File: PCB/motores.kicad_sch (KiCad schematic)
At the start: 30 parts, among them IC2 IR2175STRPBF, J10 Conn_01x03, J11 Conn_01x03, J12 motor_dc, J9 motor_lineal, K1 G6E, K2 G6E, K3 G6E, K4 G6E, Q1 AO3401A, Q2 AO3401A, Q3 AO3401A, Q4 AO3401A

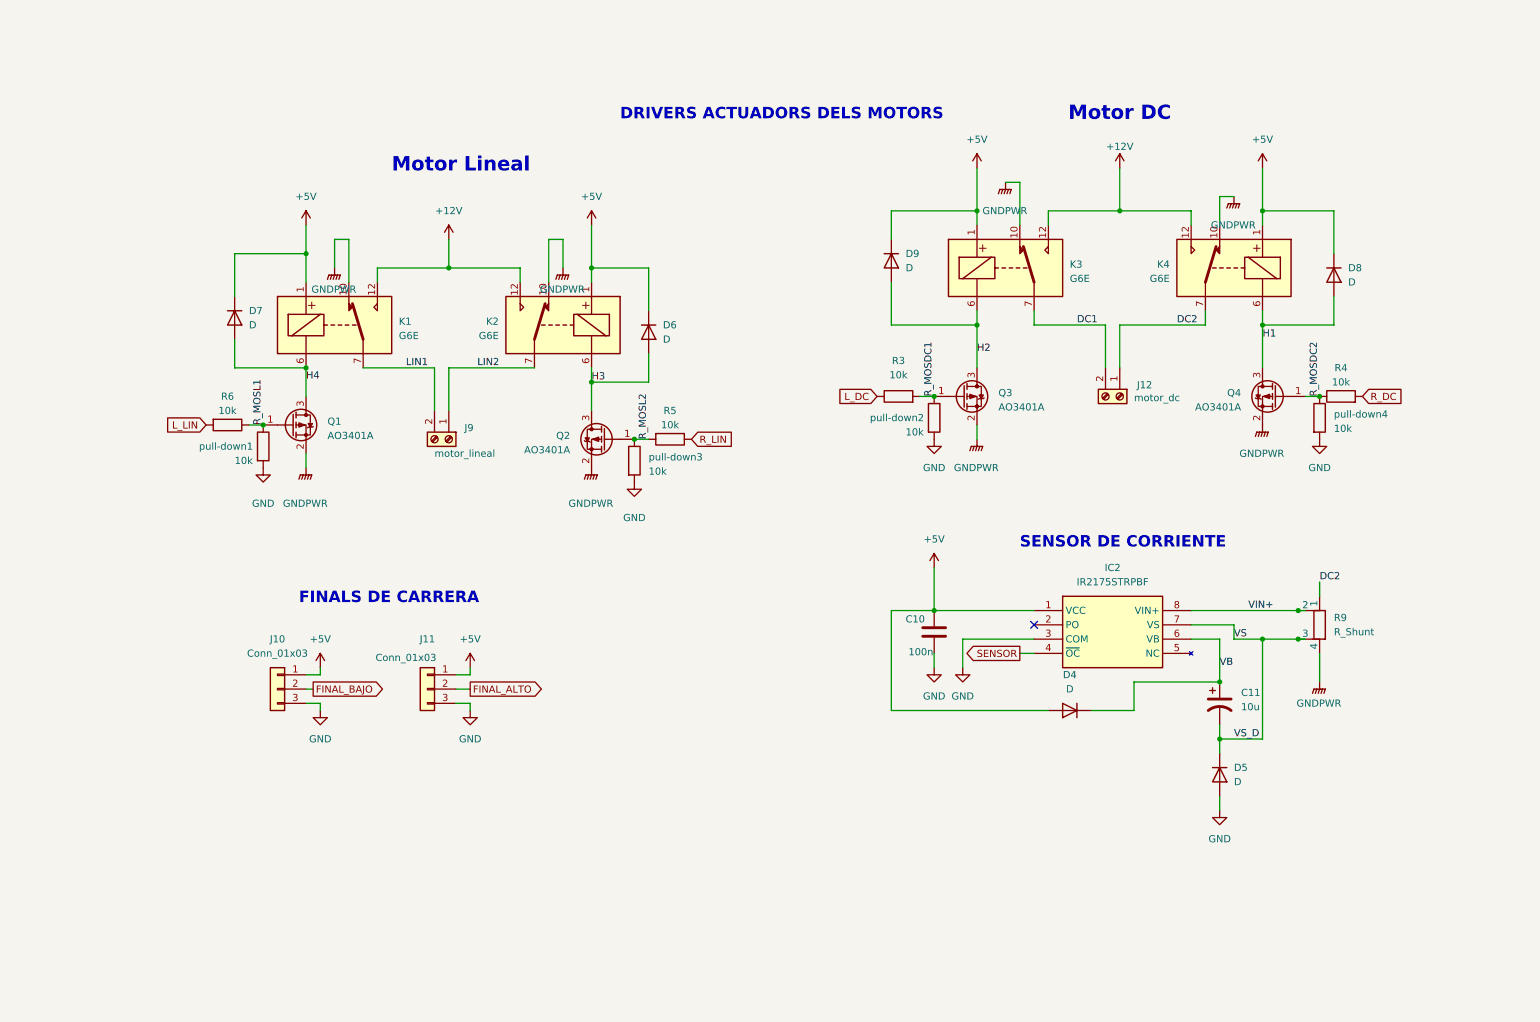
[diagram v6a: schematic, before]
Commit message: Fixed motors
mosfet shcematic fix
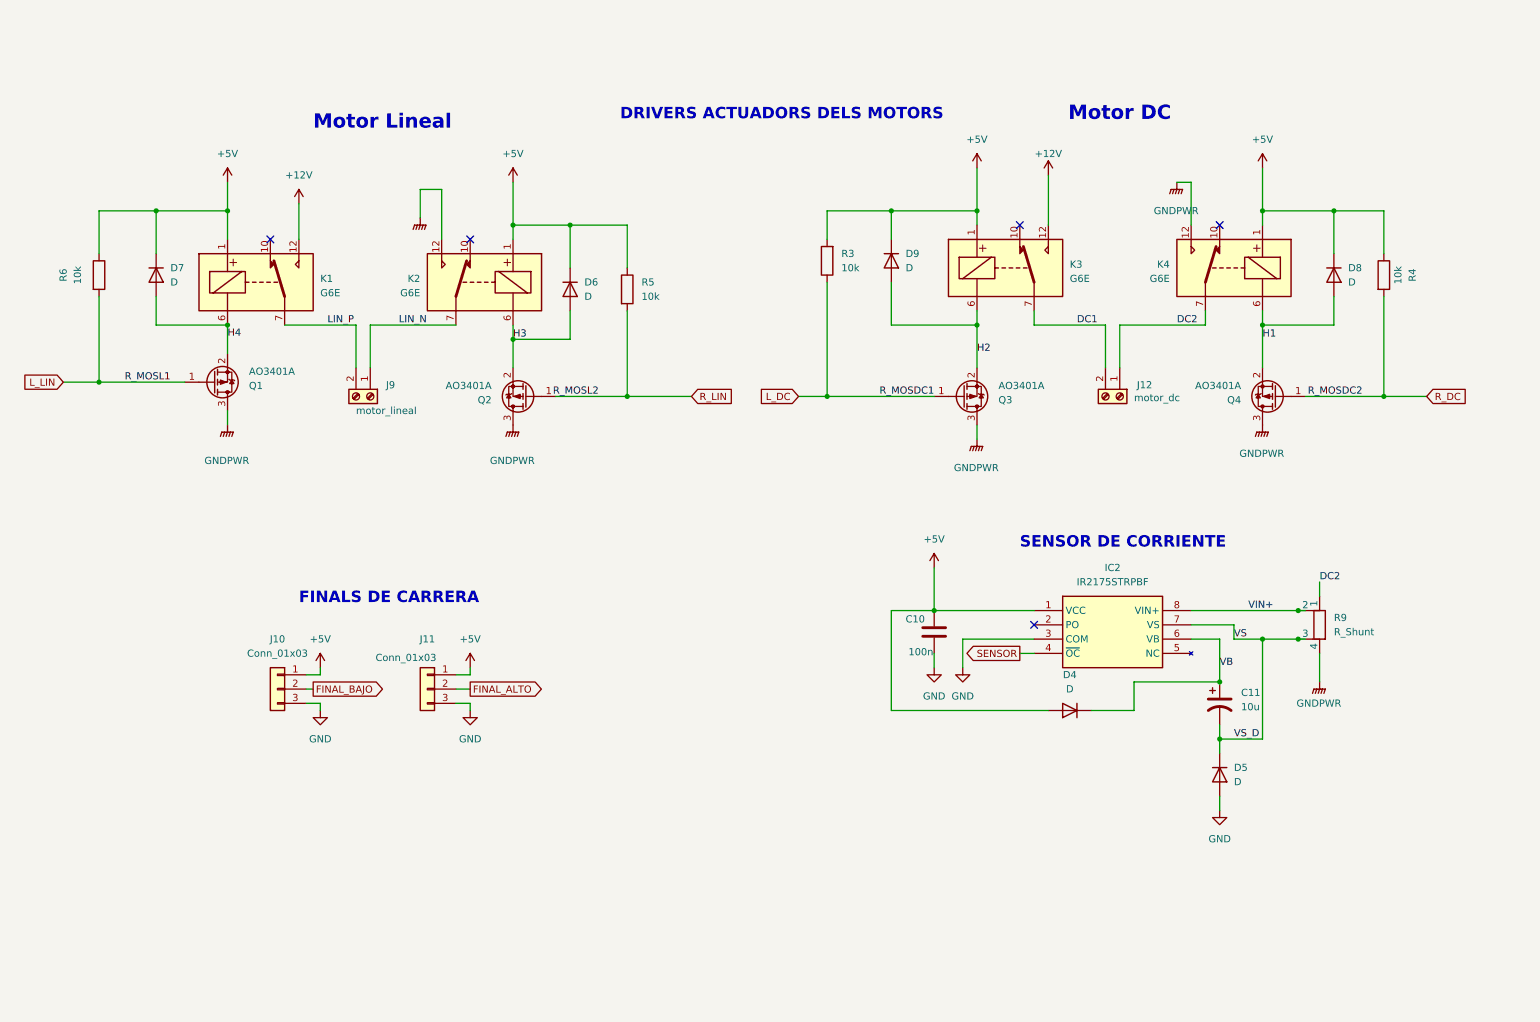
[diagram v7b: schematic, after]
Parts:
- removed pull-down1, pull-down2, pull-down3, pull-down4: 10k, Capacitor_SMD:C_1206_3216Metric, symbol Device:R
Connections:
- net R_MOSL2 is gone; now on net R_LIN: Q2.1 (G), R5.2
- net +12V: no longer K2.12, K4.12
- net +5V: now also R3.2, R4.1, R5.1, R6.1
- net GNDPWR: now also K2.12, K4.12, Q1.3 (D), Q2.3 (D), Q3.3 (D), Q4.3 (D); no longer K1.10, K2.10, K3.10, K4.10, Q1.2 (S), Q2.2 (S), Q3.2 (S), Q4.2 (S)
- net H1: now also Q4.2 (S); no longer Q4.3 (D)
- net H2: now also Q3.2 (S); no longer Q3.3 (D)
- net H3: now also Q2.2 (S); no longer Q2.3 (D)
- net H4: now also Q1.2 (S); no longer Q1.3 (D)
- net L_DC: now also Q3.1 (G)
- net L_LIN: now also Q1.1 (G)
- net R_DC: now also Q4.1 (G)
- net R_LIN: no longer R5.1
- net LIN1 renamed LIN_P
- net LIN2 renamed LIN_N
- removed net R_MOSDC1: Q3.1 (G), R3.2
- removed net R_MOSDC2: Q4.1 (G), R4.1
- removed net R_MOSL1: Q1.1 (G), R6.1
- no-connect marks 1 -> 5
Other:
- moved on the sheet: D6, D7, J9, K1, K2, Q1, Q2, Q4, R3, R4, R5, R6

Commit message: Add files via upload
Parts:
- added pull-down1, pull-down2, pull-down3, pull-down4: 10k, Capacitor_SMD:C_1206_3216Metric, symbol Device:R
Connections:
- net +12V: now also K2.12, K4.12
- net +5V: no longer R3.2, R4.1, R5.1, R6.1
- net GND: now also pull-down1.2, pull-down2.2, pull-down3.2, pull-down4.2
- net GNDPWR: now also K1.10, K2.10, K3.10, K4.10, Q1.2 (S), Q2.2 (S), Q3.2 (S), Q4.2 (S); no longer K2.12, K4.12, Q1.3 (D), Q2.3 (D), Q3.3 (D), Q4.3 (D)
- net H1: now also Q4.3 (D); no longer Q4.2 (S)
- net H2: now also Q3.3 (D); no longer Q3.2 (S)
- net H3: now also Q2.3 (D); no longer Q2.2 (S)
- net H4: now also Q1.3 (D); no longer Q1.2 (S)
- net L_DC: no longer Q3.1 (G)
- net L_LIN: no longer Q1.1 (G)
- net R_DC: no longer Q4.1 (G)
- net R_LIN: now also R5.1; no longer Q2.1 (G), R5.2
- net LIN_N renamed LIN2
- net LIN_P renamed LIN1
- new net R_MOSDC1: Q3.1 (G), R3.2, pull-down2.1
- new net R_MOSDC2: Q4.1 (G), R4.1, pull-down4.1
- new net R_MOSL1: Q1.1 (G), R6.1, pull-down1.1
- new net R_MOSL2: Q2.1 (G), R5.2, pull-down3.1
- no-connect marks 5 -> 1
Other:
- moved on the sheet: D6, D7, J9, K1, K2, Q1, Q2, Q4, R3, R4, R5, R6
